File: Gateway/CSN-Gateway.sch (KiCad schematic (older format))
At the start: 65 parts, among them IC1 ATMEGA328-A, IC2 FT232RL, P1 USB_MINI, P2 CONN_01X02, P3 CONN_ICSP, P4 CONN_OLED_SCREEN, P5 YHDC_SCT-013, P6 YHDC_SCT-013, P7 YHDC_SCT-013, P8 CONN_NRF24L01, P9 CONN_RS485, Q1 2N2222, SW1 SW_PUSH, SW2 SW_PUSH, U1 MAX485CSA, U2 AMS1117-3.3V, U3 ATSHA204A, Y1 Crystal

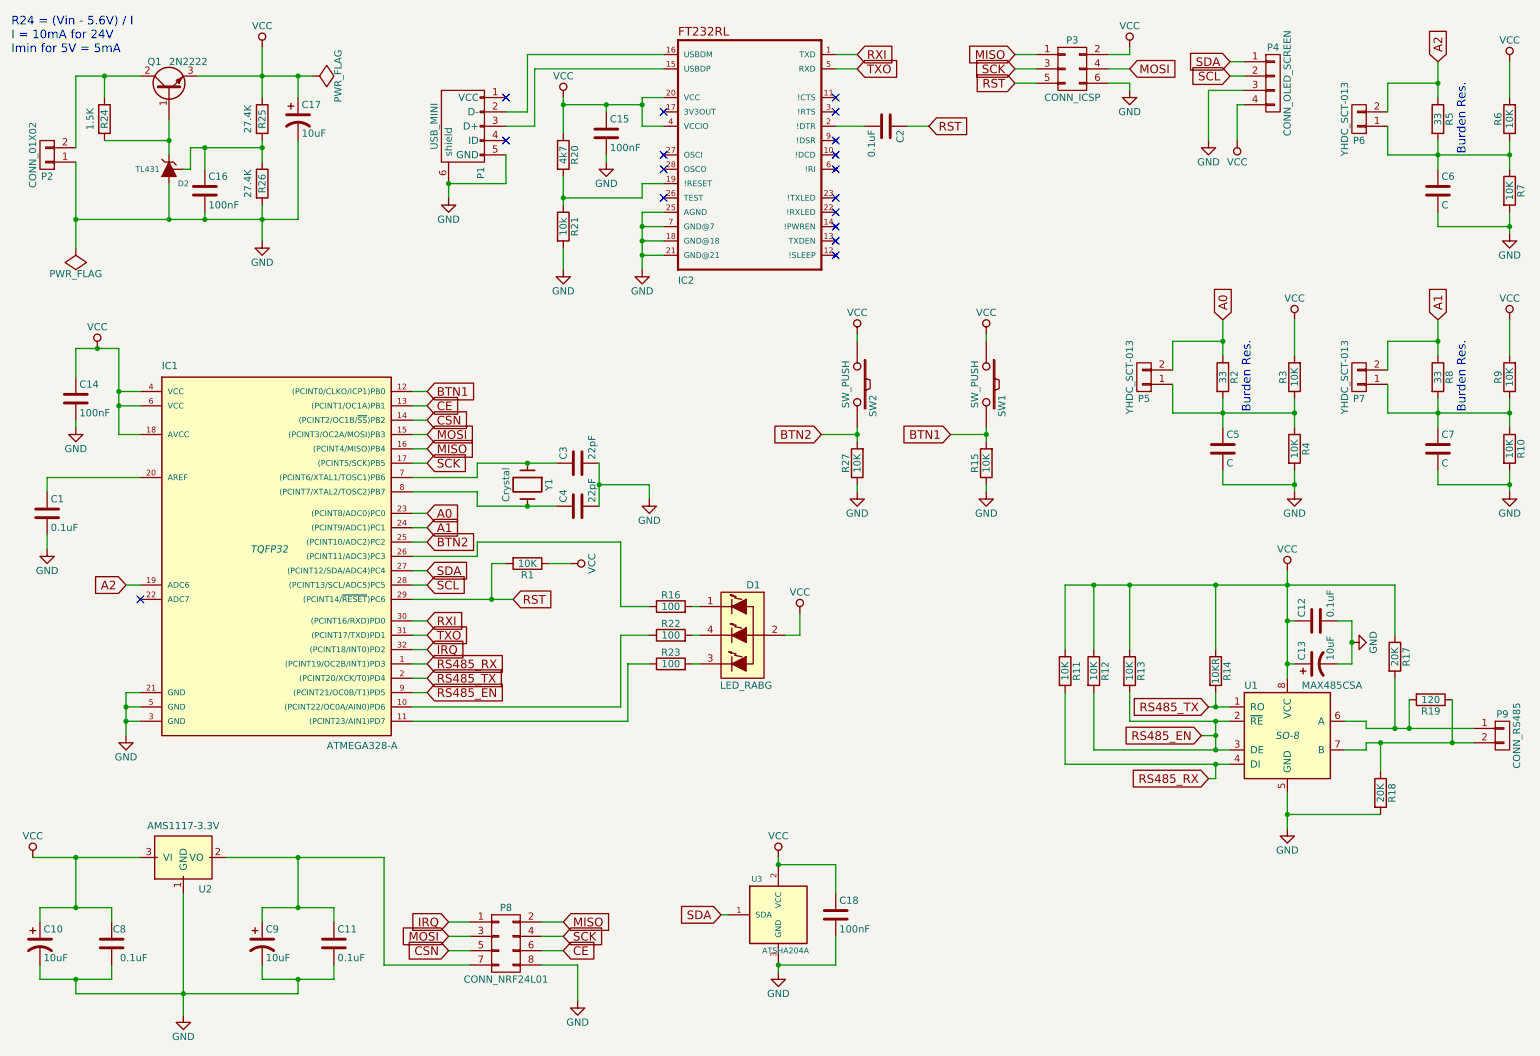
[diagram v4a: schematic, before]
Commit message: Fix ft232 self powered schematic
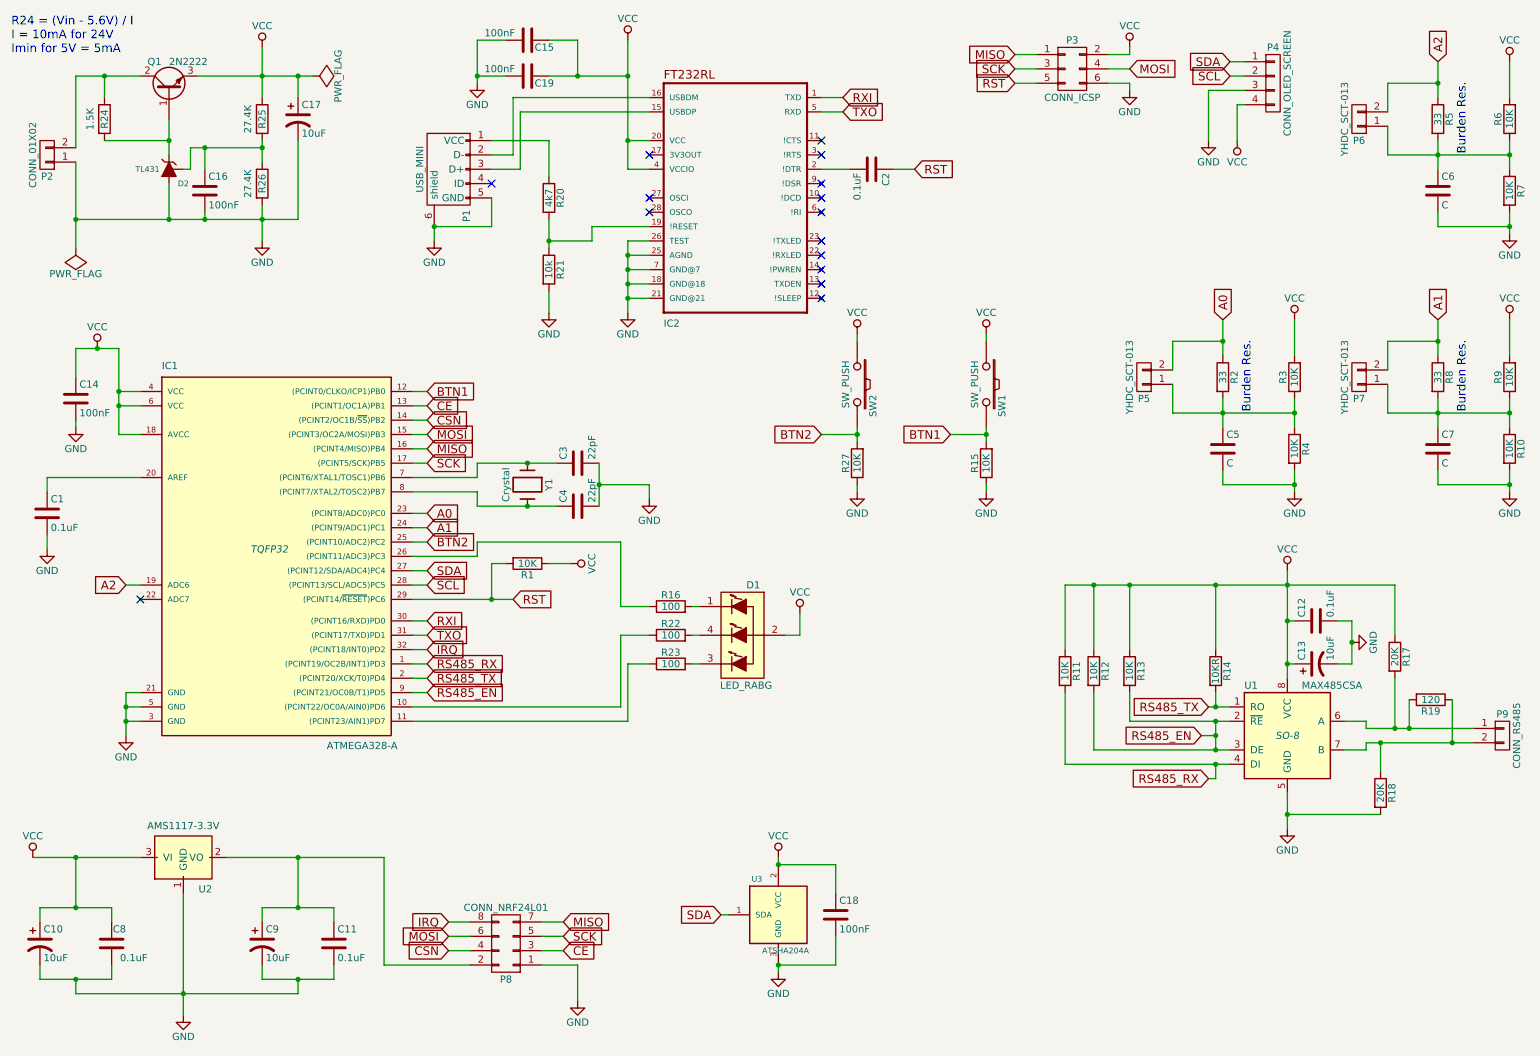
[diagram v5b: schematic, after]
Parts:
- added C19: 100nF, symbol C
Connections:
- net CE: now also P8.3 (P3); no longer P8.6 (P6)
- net CSN: now also P8.4 (P4); no longer P8.5 (P5)
- net GND: now also IC2.26 (TEST), P8.1 (P1), C19.2; no longer P8.8 (P8)
- net IRQ: now also P8.8 (P8); no longer P8.1 (P1)
- net MISO: now also P8.7 (P7); no longer P8.2 (P2)
- net MOSI: now also P8.6 (P6); no longer P8.3 (P3)
- net SCK: now also P8.5 (P5); no longer P8.4 (P4)
- net VCC: now also C19.1; no longer R20.1
- net at C11.1, C9.1, U2.2 (VO): now also P8.2 (P2); no longer P8.7 (P7)
- net at P1.1 (VCC): now also R20.1
- no-connect marks 17 -> 15
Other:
- moved on the sheet: C15, C2, IC2, P1, R20, R21

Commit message: add some pcb footprint
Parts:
- C1, C10, C11, C12, C13, C14, C15, C16, C17, C18, C19, C2, C3, C4, C8, C9: footprint (none) -> Capacitors_SMD:C_1206_HandSoldering
- C5, C6, C7: value C -> 10uF; footprint (none) -> Capacitors_SMD:C_1206_HandSoldering
- D1: footprint (none) -> footprints:LED-0606
- D2, Q1: footprint (none) -> TO_SOT_Packages_SMD:SOT-23
- IC1: footprint TQFP32 -> Housings_QFP:TQFP-32_7x7mm_Pitch0.8mm
- IC2: footprint SSOP28-LD -> Housings_SSOP:SSOP-28_5.3x10.2mm_Pitch0.65mm
- R1, R10, R11, R12, R13, R14, R15, R16, R17, R18, R19, R2, R20, R21, R22, R23, R24, R25, R26, R27, R3, R4, R5, R6, R7, R8, R9: footprint (none) -> Resistors_SMD:R_1206_HandSoldering
- U1: footprint SO-8 -> Power_Integrations:SO-8
- U2: footprint (none) -> TO_SOT_Packages_SMD:SOT-223
- U3: footprint SOT-23_Handsoldering -> TO_SOT_Packages_SMD:SOT-23_Handsoldering

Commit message: change to 0806
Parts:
- C1, C10, C11, C12, C13, C14, C15, C16, C17, C18, C19, C2, C3, C4, C5, C6, C7, C8, C9: footprint Capacitors_SMD:C_1206_HandSoldering -> Capacitors_SMD:C_0805_HandSoldering
- R1, R10, R11, R12, R13, R14, R15, R16, R17, R18, R19, R2, R20, R21, R22, R23, R24, R25, R26, R27, R3, R4, R5, R6, R7, R8, R9: footprint Resistors_SMD:R_1206_HandSoldering -> Resistors_SMD:R_0805_HandSoldering

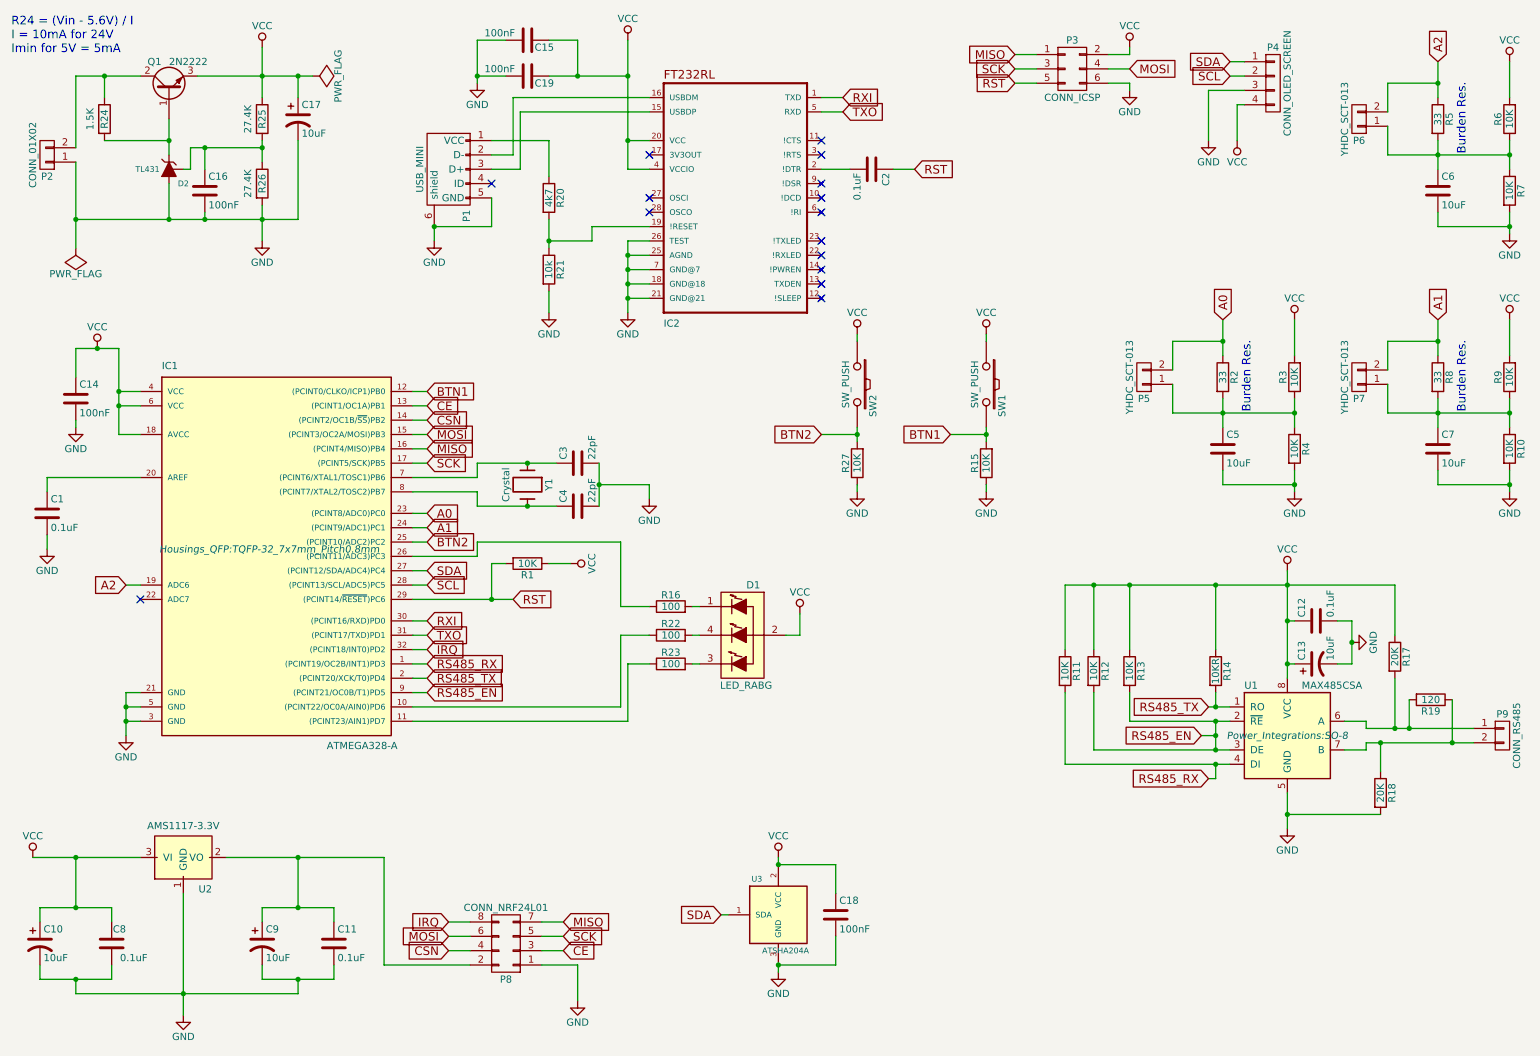
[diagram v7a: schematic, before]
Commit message: add some components
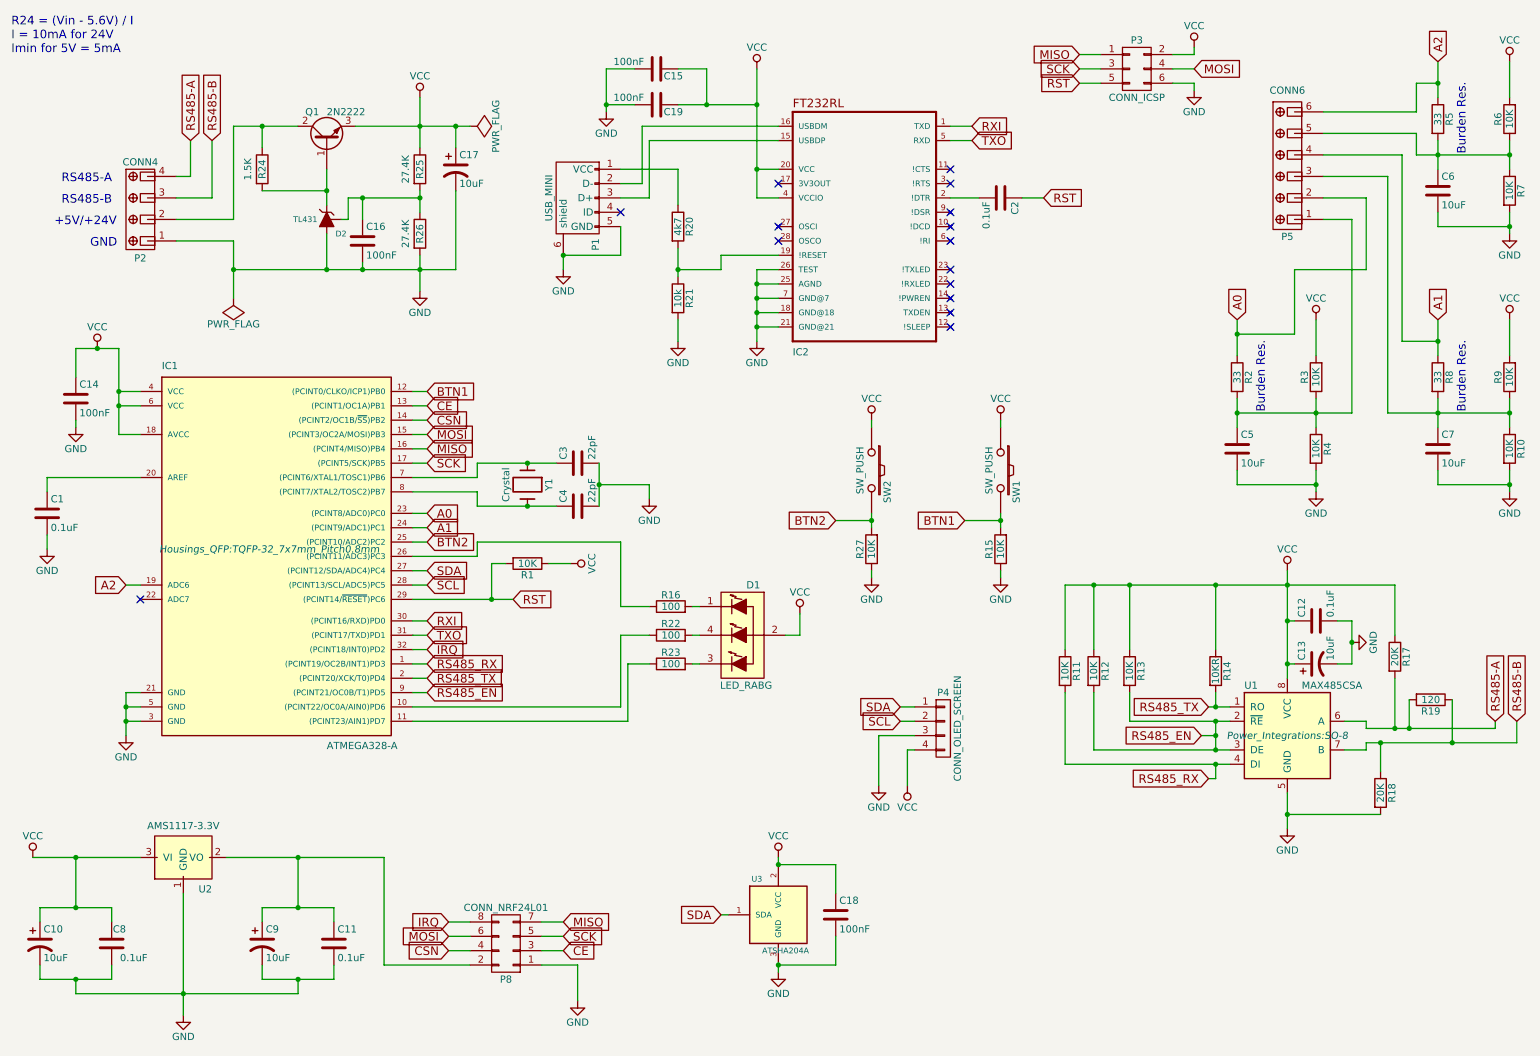
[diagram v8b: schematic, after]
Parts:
- removed P2: CONN_01X02, symbol CONN_01X02
- removed P5, P6, P7: YHDC_SCT-013, symbol CONN_01X02
- removed P9: CONN_RS485, symbol CONN_01X02
- added P2: CONN4, symbol CONN4
- added P5: CONN6, symbol CONN6
- D1: footprint footprints:LED-0606 -> (none)
- P3: footprint (none) -> Pin_Headers:Pin_Header_Straight_2x03
- P8: footprint (none) -> mysensors_radios:NRF24L01
- Y1: footprint (none) -> mysensors_obscurities:XTAL_3.2x1.5mm
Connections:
- net A0: now also P5.2
- net A1: now also P5.4
- net A2: now also P5.6
- net GND: now also P2.1
- net at Q1.2 (C), R24.1: now also P2.2
- net at C5.1, R2.2, R3.1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: now also P5.1
- net at C7.1, R10.1, R8.2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: now also P5.3
- net at C6.1, R5.2, R6.1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: now also P5.5
- net RS485-A: now reaches R17.2, R19.2, U1.6 (A)
- net RS485-A: now also P2.4
- net RS485-B: now reaches R18.1, R19.1, U1.7 (B)
- net RS485-B: now also P2.3
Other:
- note added: "+5V/+24V"
- note added: "GND"
- note added: "RS485-A"
- note added: "RS485-B"
- moved on the sheet: C15, C16, C17, C19, C2, C5, D2, IC2, P1, P3, P4, Q1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
